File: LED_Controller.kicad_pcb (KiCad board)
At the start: 2 copper layers, 127 x 101.6 mm, 37 parts, among them CON1 CONNECTOR, CON2 CONNECTOR, CON3 CONNECTOR, CON4 CONNECTOR, CON5 PWR_CON, CON6 AVR-ISP-10, CON7 AVR-ISP-6, IC1 ATMEGA328P-P, Q1 STS8DN3LLH5, Q2 STS8DN3LLH5, Q3 STS8DN3LLH5

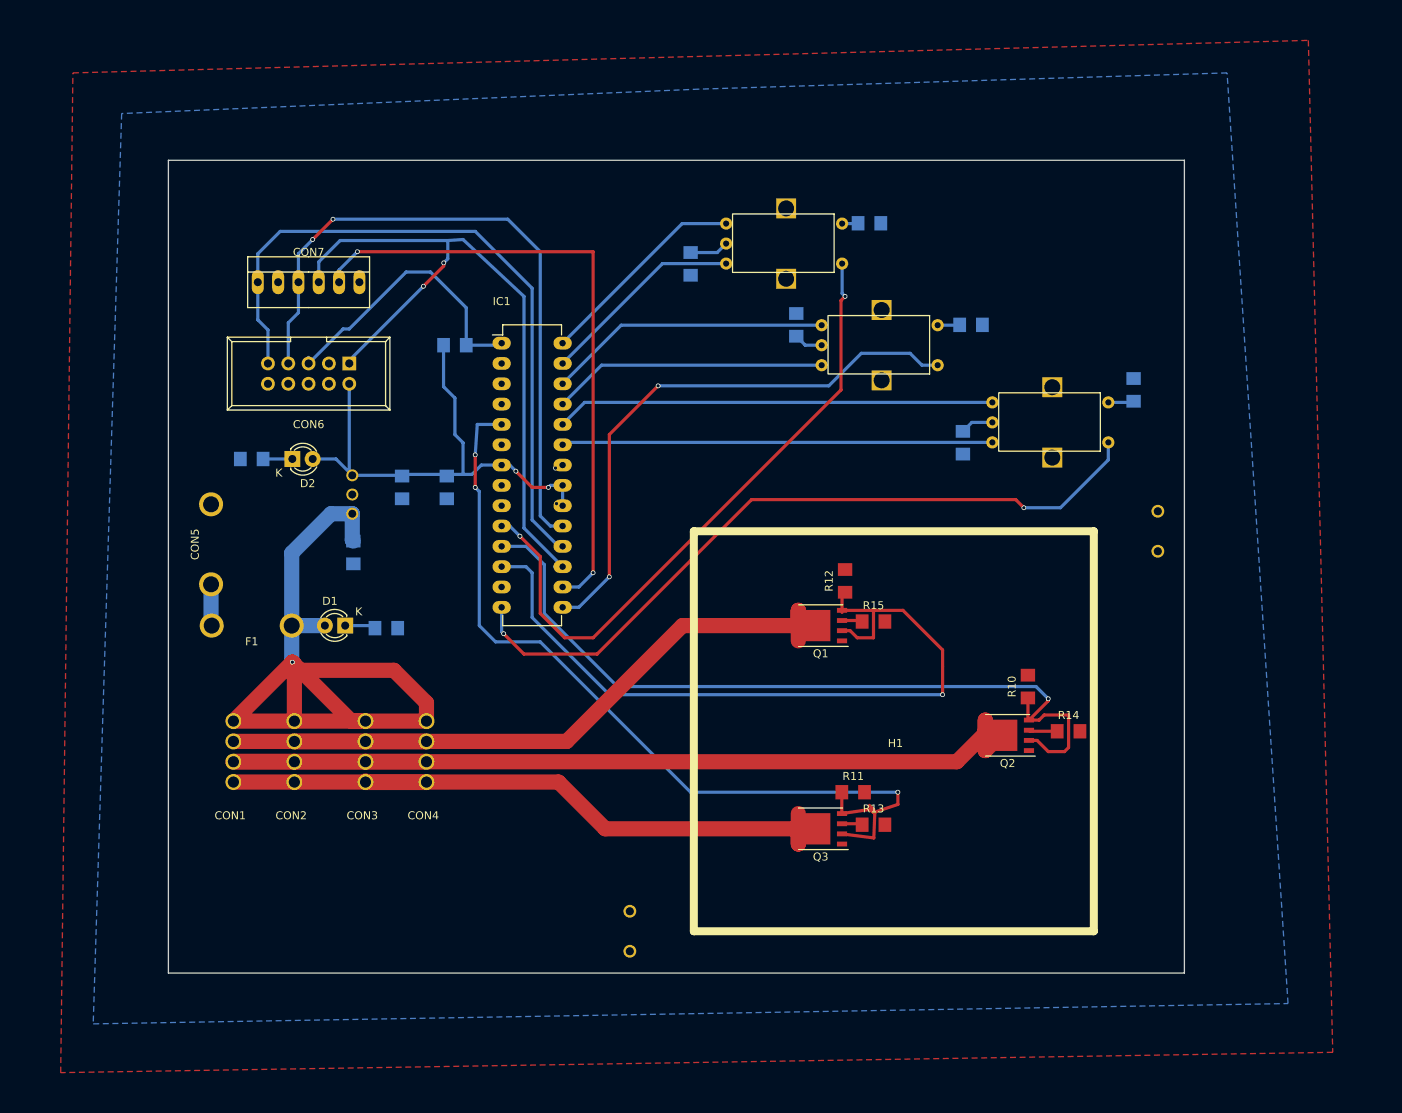
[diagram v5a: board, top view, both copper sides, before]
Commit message: Changed some encoder pins, wired outputs for I2C instead os SPI, generated gerber for milling
Re-adjusted resistors to ensure proper milling

Removed 6-pin header for SPI

Added schematic and component for 2-terminal screw block

Wired SCL and SDA to terminal block, added another terminal block for
GND and +5V and routed traces

Re-wired and traced pins for rotary encoder 3 to PD0 and PD1 (they were
connected to SCL and SDA before)

Generated Gerber files for milling
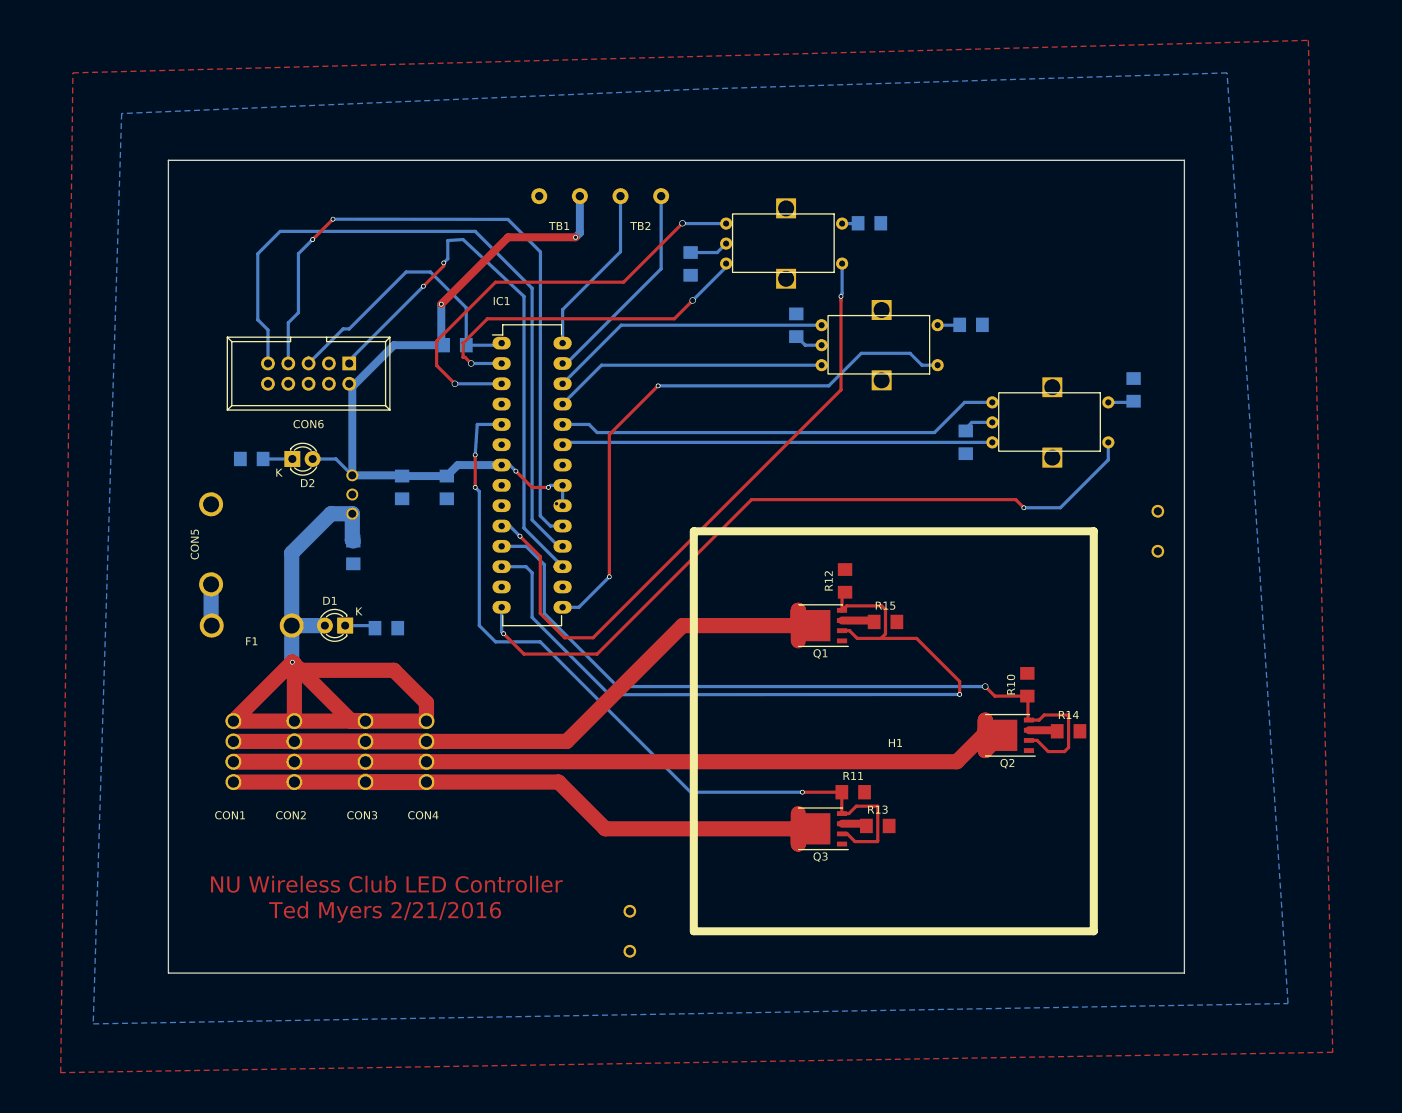
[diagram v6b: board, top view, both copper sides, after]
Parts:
- removed CON7: AVR-ISP-6, Connect:PINHEAD1-6
- added TB1: Terminal_Block_2pin, LED_controller_footprints:Screw_Terminal, F.Cu at (126.4, 59.1)
- added TB2: Terminal_Block_2pin, LED_controller_footprints:Screw_Terminal, F.Cu at (136.5, 59.1)
- moved R15 1.50 mm to (167.1, 109.8)
- moved R13 0.55 mm to (166.1, 135.3)
- moved R1 0.36 mm to (177.1, 87.3)
- moved R10 0.24 mm to (184.8, 117.6)
- moved R2 0.05 mm to (156.0, 72.7)
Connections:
- CON6 pad 3: Net-(CON6-Pad3) -> (no net)
- IC1 pad 13: Net-(IC1-Pad13) -> (no net)
- IC1 pad 16: /SS -> (no net)
- IC1 pad 2: Net-(IC1-Pad2) -> Net-(E3-Pad4)
- IC1 pad 27: Net-(E3-Pad4) -> /SDA
- IC1 pad 28: Net-(E3-Pad5) -> /SCL
- IC1 pad 3: Net-(IC1-Pad3) -> Net-(E3-Pad5)
- IC1 pad 4: Net-(IC1-Pad4) -> (no net)
- IC1 pad 6: Net-(IC1-Pad6) -> (no net)
- IC1 pad 9: Net-(IC1-Pad9) -> (no net)
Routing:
- net /SS: track 78.9 -> 0.00 mm, vias 2 -> 0
- net Net-(E3-Pad5): track 26.6 -> 54.4 mm, vias 0 -> 2
- net +5V: track 65.2 -> 92.7 mm, vias 3 -> 5
- net /SDA: track 0.00 -> 26.3 mm
- net /SCL: track 0.00 -> 21.4 mm
- net /MOSI: track 89.4 -> 69.6 mm
- net Net-(E3-Pad4): track 25.6 -> 44.2 mm, vias 0 -> 2
- net /RED_5V: track 108.1 -> 99.1 mm
- net /GREEN_5V: track 101.9 -> 95.5 mm
- net GND: track 8.72 -> 12.5 mm, vias 1 -> 0
- net /BLUE_5V: track 95.4 -> 98.0 mm
- net /MISO: track 87.8 -> 86.8 mm
- net Net-(E1-Pad5): track 54.9 -> 55.7 mm
- net (no net): track 0.75 -> 0.00 mm
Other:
- net class 1mm: clearance 0.45 -> 0.4
- net class Default: clearance 0.45 -> 0.4
- net class HIGH_CURRENT: clearance 0.45 -> 0.4
- rule trace_clearance: 0.45 -> 0.4
- board text added: "NU Wireless Club LED Controller Ted Myers 2/21/2016"

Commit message: More output pins for LED strips, mounting holes added
Updated size of LED output holes for LED strips

Added more output footprints for strips

Added mounting holes to corners of board; are probably incorrect size,
modify later

Exported updated gerbers
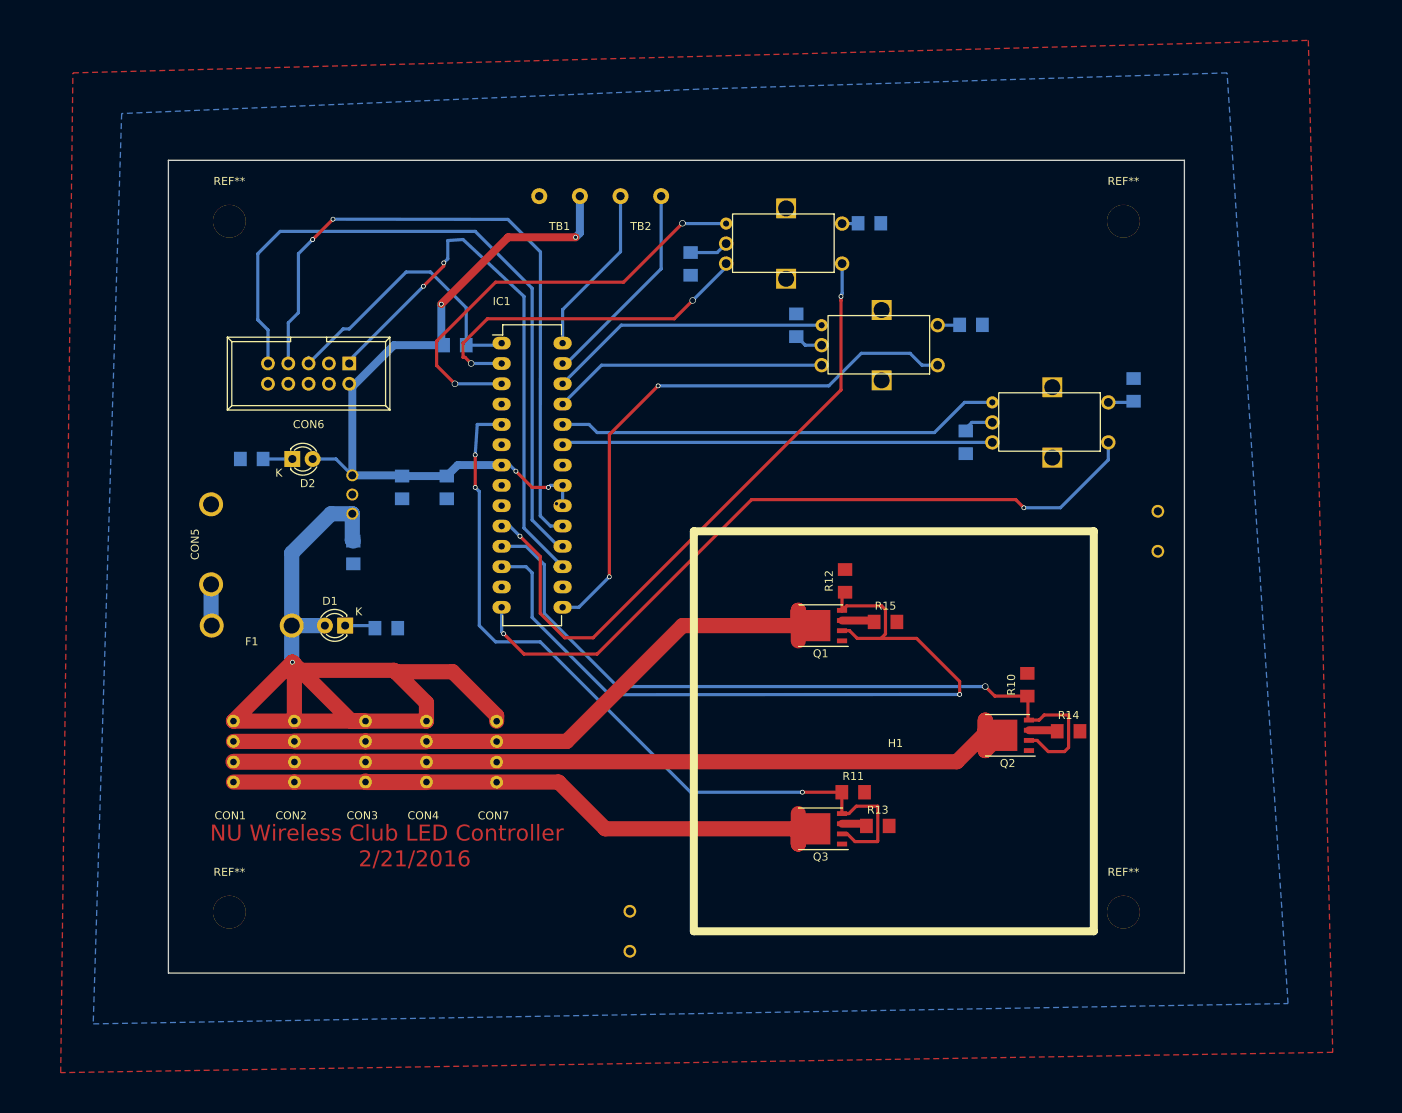
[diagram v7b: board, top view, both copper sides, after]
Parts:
- added CON7: CONNECTOR, LED_controller_footprints:OUTPUT_HOLES, F.Cu at (118.5, 126.0)
- added REF**: MOUNTING_HOLE, LED_controller_footprints:MOUNTING_HOLE, F.Cu at (85.1, 59.7)
- added REF**: MOUNTING_HOLE, LED_controller_footprints:MOUNTING_HOLE, F.Cu at (196.8, 59.7)
- added REF**: MOUNTING_HOLE, LED_controller_footprints:MOUNTING_HOLE, F.Cu at (196.8, 146.1)
- added REF**: MOUNTING_HOLE, LED_controller_footprints:MOUNTING_HOLE, F.Cu at (85.1, 146.1)
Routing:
- net +12V: track 104.8 -> 120.5 mm
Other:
- board text added: "NU Wireless Club LED Controller 2/21/2016"
- board text removed: "NU Wireless Club LED Controller Ted Myers 2/21/2016"

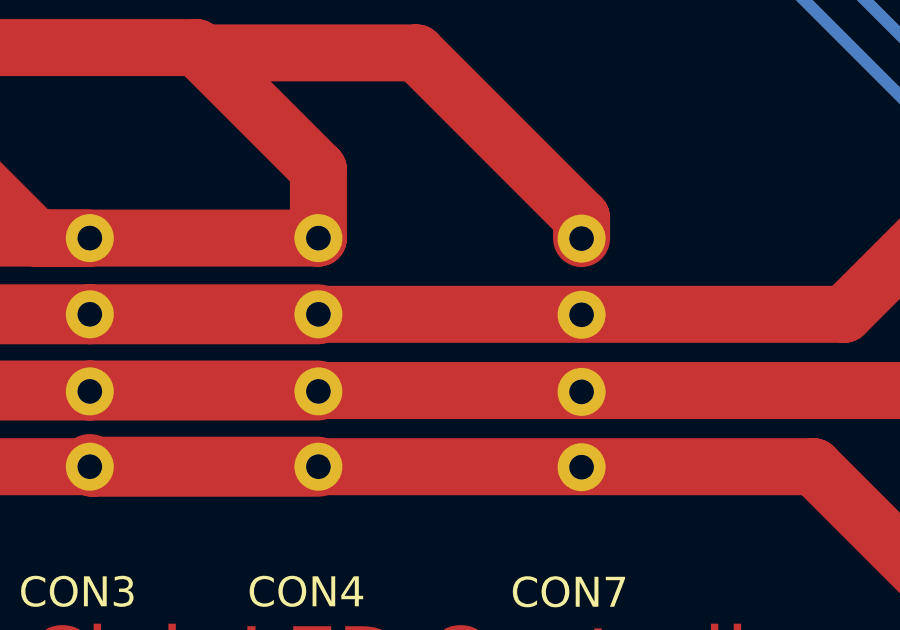
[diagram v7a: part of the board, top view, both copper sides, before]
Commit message: Quick Fixes
Connected unconnected trace to one of the LED strip holes

Re-exported Gerber files
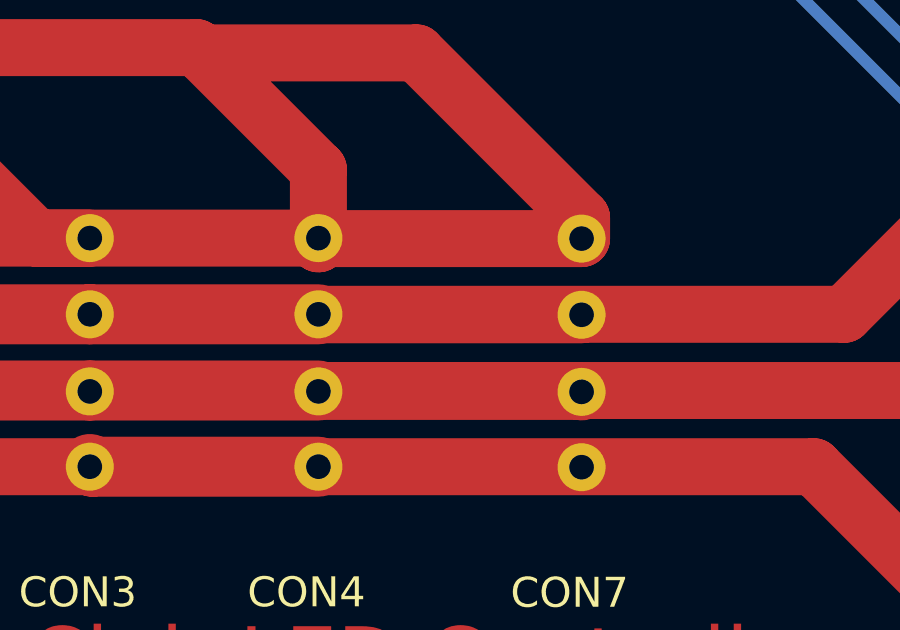
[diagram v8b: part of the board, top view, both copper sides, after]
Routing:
- net +12V: track 120.5 -> 129.5 mm
- net /BLUE_PWR: track 88.2 -> 97.0 mm
- net /GREEN_PWR: track 106.6 -> 115.4 mm
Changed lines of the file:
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@@
   (general
     (links 112)
-    (no_connects 6)
+    (no_connects 4)
     (area 64.008 37.084 223.012001 166.116001)
     (thickness 1.6)
     (drawings 5)
-    (tracks 300)
+    (tracks 307)
     (zones 0)
     (modules 43)
@@
   (segment (start 164.46754 135.001) (end 164.77234 135.3058) (width 0.4) (layer F.Cu) (net 2))
   (segment (start 185.169 123.444) (end 185.042 123.317) (width 0.4) (layer F.Cu) (net 2))
+  (segment (start 118.5 122.19) (end 109.901998 122.19) (width 1.9) (layer F.Cu) (net 3))
+  (segment (start 109.901998 122.19) (end 109.728 122.363998) (width 1.9) (layer F.Cu) (net 3))
+  (segment (start 109.728 122.363998) (end 109.728 122.174) (width 1.9) (layer F.Cu) (net 3))
   (segment (start 118.5 122.19) (end 118.5 121.5) (width 1.9) (layer F.Cu) (net 3))
   (segment (start 118.5 121.5) (end 113 116) (width 1.9) (layer F.Cu) (net 3))
@@
   (segment (start 109.728 129.794) (end 102.197998 129.794) (width 2) (layer F.Cu) (net 25) (status 30))
   (segment (start 102.197998 129.794) (end 102.108 129.704002) (width 2) (layer F.Cu) (net 25) (status 30))
+  (segment (start 109.728 127.284) (end 118.484 127.284) (width 1.9) (layer F.Cu) (net 26))
+  (segment (start 118.484 127.284) (end 118.5 127.3) (width 1.9) (layer F.Cu) (net 26))
   (segment (start 179.577 122.047) (end 179.577 123.317) (width 1.9) (layer F.Cu) (net 26) (status 30))
   (segment (start 179.577 123.317) (end 179.577 124.587) (width 1.9) (layer F.Cu) (net 26) (status 30))
@@
   (segment (start 102.108 127.254) (end 93.218 127.254) (width 2) (layer F.Cu) (net 26) (status 30))
   (segment (start 93.218 127.254) (end 85.598 127.254) (width 2) (layer F.Cu) (net 26) (status 30))
+  (segment (start 118.5 124.73) (end 109.744 124.73) (width 1.9) (layer F.Cu) (net 27))
+  (segment (start 109.744 124.73) (end 109.728 124.714) (width 1.9) (layer F.Cu) (net 27))
   (segment (start 156.209 109.601) (end 156.209 110.871) (width 1.9) (layer F.Cu) (net 27) (status 30))
   (segment (start 156.209 110.871) (end 156.209 108.331) (width 1.9) (layer F.Cu) (net 27) (status 30))
